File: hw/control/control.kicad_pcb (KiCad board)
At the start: 2 copper layers, 160 x 90 mm, 146 parts, among them J101 Screw_Terminal_01x02, J102 Screw_Terminal_01x03, J103 Screw_Terminal_01x03, J301 Conn_02x05_Odd_Even, J302 Conn_01x04, J303 Raspberry_Pi_0_2_3, J304 Micro_SD_Card, J305 Conn_01x06, J306 Conn_01x07, Q1001 BC807, Q1002 BC817, Q401 BC817, Q501 BC817, Q601 BC817, Q701 BC817, Q801 BC807, Q802 BC817, Q901 AOSP21357, Q902 IRF4905, SW301 SW_Push, U1001 LM2678T-ADJ, U1101 SN74AHCT125D, U201 LM2596T-ADJ, U801 LM2678T-ADJ

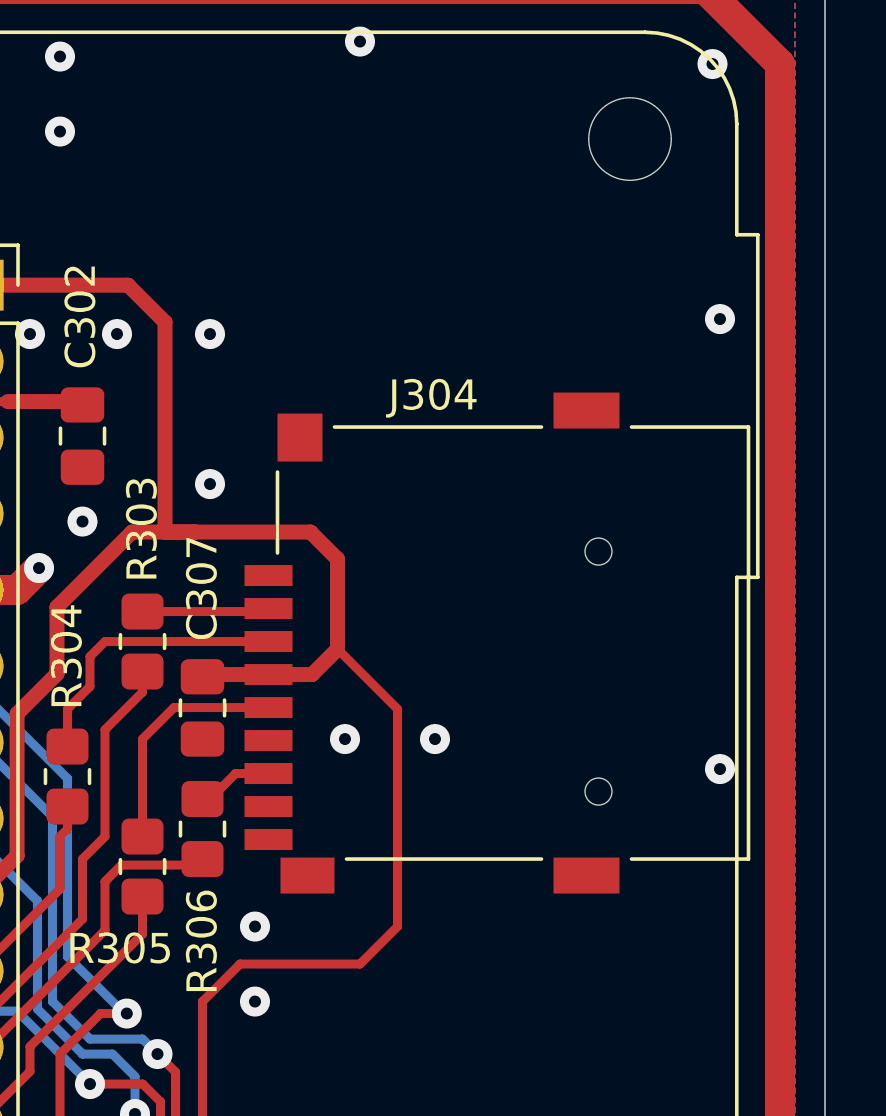
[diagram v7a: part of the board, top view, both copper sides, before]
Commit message: [hw] Isolate SD card holder shield from ground
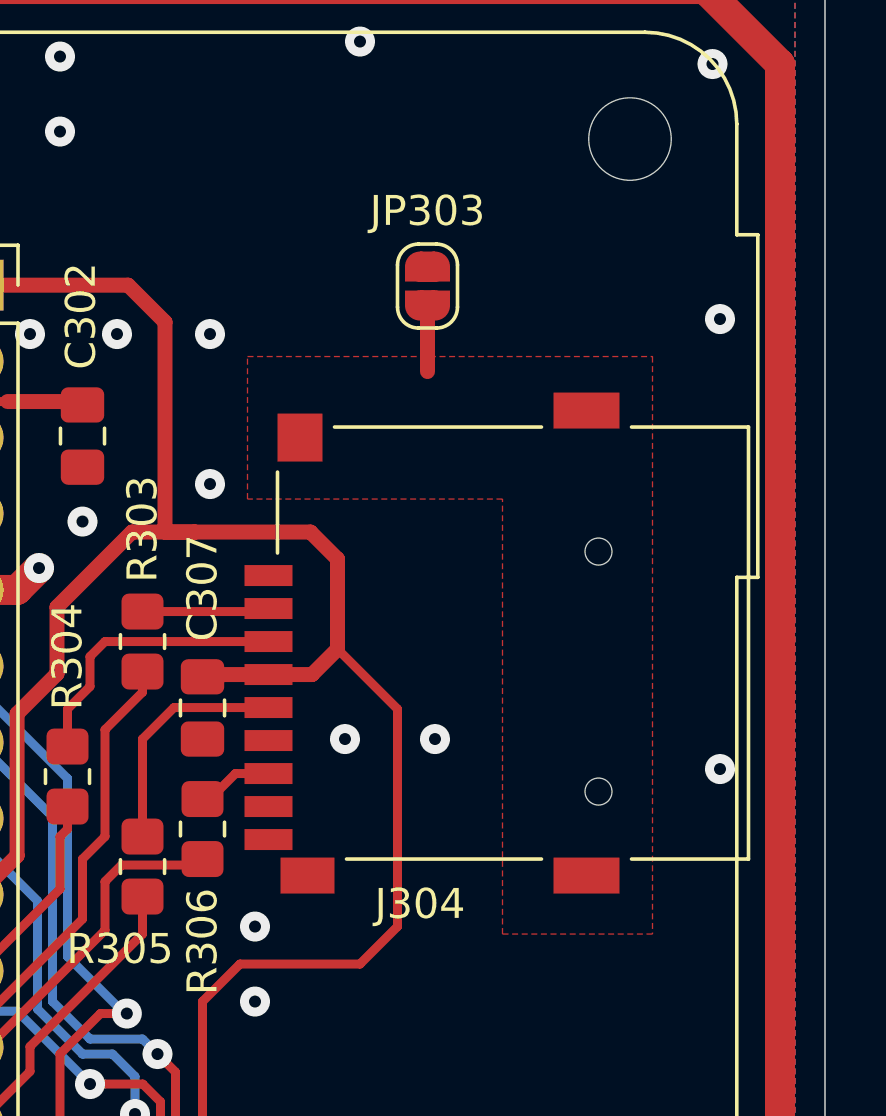
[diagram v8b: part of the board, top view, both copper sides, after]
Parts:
- added JP303: SolderJumper_2_Open, Jumper:SolderJumper-2_P1.3mm_Open_RoundedPad1.0x1.5mm, F.Cu at (206.8, 61.4)
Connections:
- J304 pad 9: GND -> Net-(J304-Pad9)
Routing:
- net Net-(J304-Pad9): track 0.00 -> 2.20 mm
- added copper zone on F.Cu, net Net-(J304-Pad9)
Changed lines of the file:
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@@
     (thickness 1.6)
     (drawings 4)
-    (tracks 1677)
+    (tracks 1678)
     (zones 0)
-    (modules 146)
-    (nets 93)
+    (modules 147)
+    (nets 94)
   )
   (page A4)
@@
     (mod_text_size 1 1)
     (mod_text_width 0.15)
-    (pad_size 3.6 1.7)
+    (pad_size 1.2 1.8)
     (pad_drill 0)
     (pad_to_mask_clearance 0.1)
@@
   (net 91 "Net-(J306-Pad4)")
   (net 92 "Net-(J306-Pad3)")
+  (net 93 "Net-(J304-Pad9)")
   (net_class Default "This is the default net class."
     (clearance 0.2)
@@
     (add_net "Net-(J304-Pad7)")
     (add_net "Net-(J304-Pad8)")
+    (add_net "Net-(J304-Pad9)")
     (add_net "Net-(J306-Pad3)")
     (add_net "Net-(J306-Pad4)")
@@
     (add_net /LED_PWR_EN1)
   )
+  (module Jumper:SolderJumper-2_P1.3mm_Open_RoundedPad1.0x1.5mm (layer F.Cu)
+    (at 206.75 61.4 90)
+    (descr "SMD Solder Jumper, 1x1.5mm, rounded Pads, 0.3mm gap, open")
+    (tags "solder jumper open")
+    (attr virtual)
+    (fp_text reference JP303 (at 2.5 0 180) (layer F.SilkS)
+      (effects (font (size 1 1) (thickness 0.15)))
+    )
+    (fp_text value SolderJumper_2_Open (at 0 1.9 90) (layer F.Fab)
+      (effects (font (size 1 1) (thickness 0.15)))
+    )
+    (fp_line (start 1.65 1.25) (end -1.65 1.25) (layer F.CrtYd) (width 0.05))
+    (fp_line (start 1.65 1.25) (end 1.65 -1.25) (layer F.CrtYd) (width 0.05))
+    (fp_line (start -1.65 -1.25) (end -1.65 1.25) (layer F.CrtYd) (width 0.05))
+    (fp_line (start -1.65 -1.25) (end 1.65 -1.25) (layer F.CrtYd) (width 0.05))
+    (fp_line (start -0.7 -1) (end 0.7 -1) (layer F.SilkS) (width 0.12))
+    (fp_line (start 1.4 -0.3) (end 1.4 0.3) (layer F.SilkS) (width 0.12))
+    (fp_line (start 0.7 1) (end -0.7 1) (layer F.SilkS) (width 0.12))
+    (fp_line (start -1.4 0.3) (end -1.4 -0.3) (layer F.SilkS) (width 0.12))
+    (fp_arc (start -0.7 -0.3) (end -0.7 -1) (angle -90) (layer F.SilkS) (width 0.12))
+    (fp_arc (start -0.7 0.3) (end -1.4 0.3) (angle -90) (layer F.SilkS) (width 0.12))
+    (fp_arc (start 0.7 0.3) (end 0.7 1) (angle -90) (layer F.SilkS) (width 0.12))
+    (fp_arc (start 0.7 -0.3) (end 1.4 -0.3) (angle -90) (layer F.SilkS) (width 0.12))
+    (pad 2 smd custom (at 0.65 0 90) (size 1 0.5) (layers F.Cu F.Mask)
+      (net 2 GND) (zone_connect 2)
+      (options (clearance outline) (anchor rect))
+      (primitives
+        (gr_circle (center 0 0.25) (end 0.5 0.25) (width 0))
+        (gr_circle (center 0 -0.25) (end 0.5 -0.25) (width 0))
+        (gr_poly (pts
+           (xy 0 -0.75) (xy -0.5 -0.75) (xy -0.5 0.75) (xy 0 0.75)) (width 0))
+      ))
+    (pad 1 smd custom (at -0.65 0 90) (size 1 0.5) (layers F.Cu F.Mask)
+      (net 93 "Net-(J304-Pad9)") (zone_connect 2)
+      (options (clearance outline) (anchor rect))
+      (primitives
+        (gr_circle (center 0 0.25) (end 0.5 0.25) (width 0))
+        (gr_circle (center 0 -0.25) (end 0.5 -0.25) (width 0))
+        (gr_poly (pts
+           (xy 0 -0.75) (xy 0.5 -0.75) (xy 0.5 0.75) (xy 0 0.75)) (width 0))
+      ))
+  )
   (module Button_Switch_THT:SW_PUSH_6mm (layer F.Cu)
     (at 202.75 137 90)
@@
       (effects (font (size 1 1) (thickness 0.15)))
     )
-    (fp_text user %R (at 3.25 2.25 90) (layer F.Fab)
-      (effects (font (size 1 1) (thickness 0.15)))
-    )
     (fp_line (start 3.25 -0.75) (end 6.25 -0.75) (layer F.Fab) (width 0.1))
     (fp_line (start 6.25 -0.75) (end 6.25 5.25) (layer F.Fab) (width 0.1))
@@
     (fp_line (start 6.75 3) (end 6.75 1.5) (layer F.SilkS) (width 0.12))
     (fp_circle (center 3.25 2.25) (end 1.25 2.5) (layer F.Fab) (width 0.1))
+    (fp_text user %R (at 3.25 2.25 90) (layer F.Fab)
+      (effects (font (size 1 1) (thickness 0.15)))
+    )
     (pad 1 thru_hole circle (at 6.5 0 180) (size 2 2) (drill 1.1) (layers *.Cu *.Mask)
       (net 82 "Net-(J303-Pad31)"))
@@
       (effects (font (size 1 1) (thickness 0.15)))
     )
-    (fp_text user %R (at 0 0 90) (layer F.Fab)
-      (effects (font (size 0.5 0.5) (thickness 0.08)))
-    )
     (fp_line (start -1 0.625) (end -1 -0.625) (layer F.Fab) (width 0.1))
     (fp_line (start -1 -0.625) (end 1 -0.625) (layer F.Fab) (width 0.1))
@@
     (fp_line (start 1.85 -0.95) (end 1.85 0.95) (layer F.CrtYd) (width 0.05))
     (fp_line (start 1.85 0.95) (end -1.85 0.95) (layer F.CrtYd) (width 0.05))
+    (fp_text user %R (at 0 0 90) (layer F.Fab)
+      (effects (font (size 0.5 0.5) (thickness 0.08)))
+    )
     (pad 2 smd roundrect (at 1 0 270) (size 1.2 1.4) (layers F.Cu F.Paste F.Mask) (roundrect_rratio 0.208333)
       (net 82 "Net-(J303-Pad31)"))
@@
     (at 212.45 73.3 90)
     (attr smd)
-    (fp_text reference J304 (at 8.25 -5.5 180) (layer F.SilkS)
+    (fp_text reference J304 (at -8.7 -5.95 180) (layer F.SilkS)
       (effects (font (size 1 1) (thickness 0.15)))
     )
@@
     (pad "" np_thru_hole circle (at -4.95 0 90) (size 0.9 0.9) (drill 0.9) (layers *.Cu *.Mask))
     (pad 9 smd rect (at 7.75 -0.4 90) (size 1.2 2.2) (layers F.Cu F.Paste F.Mask)
-      (net 2 GND))
+      (net 93 "Net-(J304-Pad9)"))
     (pad 9 smd rect (at 6.85 -9.95 90) (size 1.6 1.5) (layers F.Cu F.Paste F.Mask)
-      (net 2 GND))
+      (net 93 "Net-(J304-Pad9)"))
     (pad 9 smd rect (at -7.75 -0.4 90) (size 1.2 2.2) (layers F.Cu F.Paste F.Mask)
-      (net 2 GND))
+      (net 93 "Net-(J304-Pad9)"))
     (pad 9 smd rect (at -7.75 -9.7 90) (size 1.2 1.8) (layers F.Cu F.Paste F.Mask)
-      (net 2 GND))
+      (net 93 "Net-(J304-Pad9)"))
     (pad CD smd rect (at -6.55 -11 90) (size 0.7 1.6) (layers F.Cu F.Paste F.Mask))
     (pad 8 smd rect (at -5.45 -11 90) (size 0.7 1.6) (layers F.Cu F.Paste F.Mask)
@@
   (segment (start 185.756712 108.967046) (end 185.720971 108.910165) (width 0.3) (layer F.Cu) (net 90))
   (segment (start 183.658018 110.957345) (end 183.591262 110.964866) (width 0.3) (layer F.Cu) (net 90))
+  (segment (start 206.75 62.05) (end 206.75 64.25) (width 0.5) (layer F.Cu) (net 93))
   (zone (net 2) (net_name GND) (layer F.Cu) (hatch edge 0.508)
     (connect_pads (clearance 0.5))
@@
       )
     )
+  )
+  (zone (net 93) (net_name "Net-(J304-Pad9)") (layer F.Cu) (hatch edge 0.508)
+    (priority 1)
+    (connect_pads (clearance 0.5))
+    (min_thickness 0.254)
+    (fill yes (arc_segments 32) (thermal_gap 0.508) (thermal_bridge_width 0.508))
+    (polygon
+      (pts
+        (xy 214.25 83) (xy 209.25 83) (xy 209.25 68.5) (xy 200.75 68.5) (xy 200.75 63.75)
+        (xy 214.25 63.75)
+      )
+    )
